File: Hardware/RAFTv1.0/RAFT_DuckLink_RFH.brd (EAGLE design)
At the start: 73.7 x 86.4 mm, 147 parts, among them J1 AMPHENOL_132134, J2 AMPHENOL_132134, J4 Micro-USB, J5 132134-15, J6 S2B-PH-K-S(LF)(SN), J8 POWER_JACK, Q1 SIA817EDJ, Q2 SI7288DP, Q4 SI7288DP, U1 SX1276, U10 PE4259, U2 MAX2771ETI+, U3 ESP32-D0WD, U4 W25Q16BVSSIG, U5 INTERFACE-CP2102-GMR(QFN28), U6 PE4259, U7 SP0503BAHT, U8 BQ24650RVAR, U9 TPS63070RNMT, Y1 32.768kHz

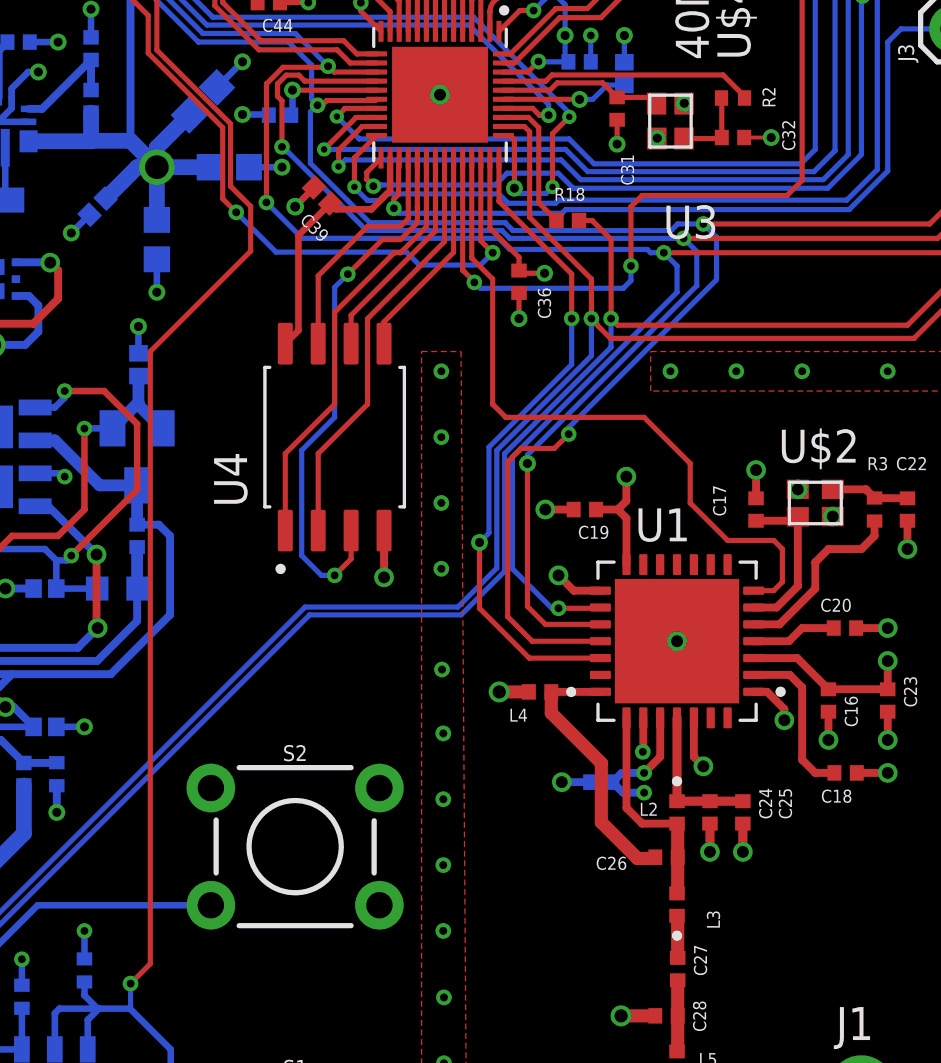
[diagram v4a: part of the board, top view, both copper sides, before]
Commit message: added connection SX1276 interrupt (remapped SX_RST to button)
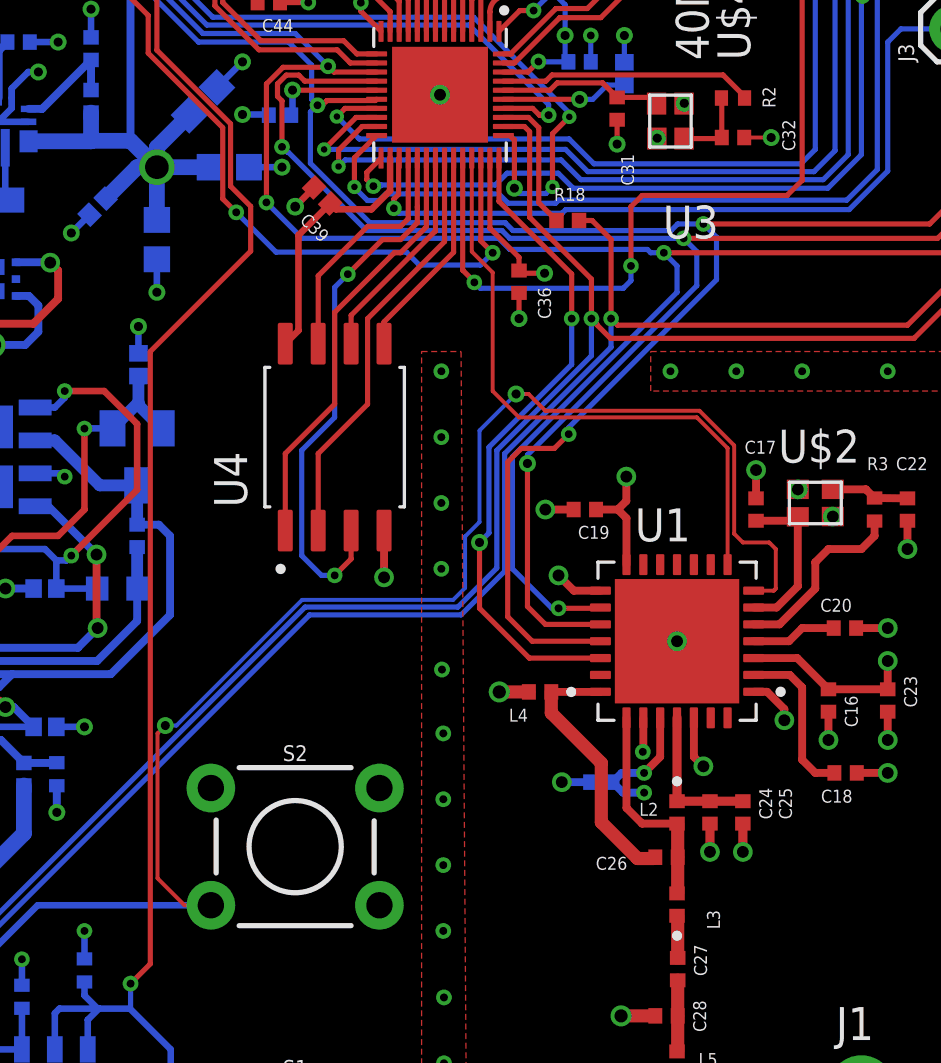
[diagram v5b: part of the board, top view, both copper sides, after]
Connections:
- removed net N$44: Q4.5, Q4.6, R24.1, S2.3
- new net SX_INT: U1.8, U3.35
- net SX_RST: now also Q4.5, Q4.6, R24.1, S2.3; no longer U3.35
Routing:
- net SX_RST: track 26.7 -> 63.3 mm, vias 0 -> 2
- net SX_INT: track 0.00 -> 23.8 mm
- net N$44: track 15.9 -> 0.00 mm
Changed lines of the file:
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@@
 <attribute name="MF" value="Murata" x="-16.51" y="-22.606" size="1.778" layer="27" rot="R270" display="off"/>
 <attribute name="MP" value="GCM1555C1H150JA16D" x="-16.51" y="-22.606" size="1.778" layer="27" rot="R270" display="off"/>
-<attribute name="NAME" x="56.764" y="35.494" size="0.5" layer="25" rot="R270"/>
+<attribute name="NAME" x="57.978" y="36.698" size="0.5" layer="25"/>
 <attribute name="PACKAGE" value="1005 Taiyo Yuden" x="-16.51" y="-22.606" size="1.778" layer="27" rot="R270" display="off"/>
 <attribute name="VALUE" x="57.79" y="35.494" size="0.5" layer="27" rot="R270" align="top-left"/>
@@
 <vertex x="47.0408" y="40.64"/>
 <vertex x="47.29330625" y="4.52269375"/>
-<vertex x="47.29330625" y="4.52269375"/>
 <vertex x="47.29330625" y="4.064"/>
 <vertex x="70.612" y="4.064"/>
@@
 <signal name="SX_RST">
 <contactref element="U1" pad="7"/>
-<contactref element="U3" pad="35"/>
-<wire x1="57.3278" y1="33.3502" x2="59.1058" y2="33.3502" width="0.2" layer="1"/>
-<wire x1="59.1058" y1="33.3502" x2="59.436" y2="33.02" width="0.2" layer="1"/>
-<wire x1="59.436" y1="33.02" x2="59.436" y2="31.75" width="0.2" layer="1"/>
-<wire x1="59.436" y1="31.75" x2="59.1" y2="31.414" width="0.2" layer="1"/>
-<wire x1="59.1" y1="31.414" x2="58.327" y2="31.414" width="0.2" layer="1"/>
-<wire x1="55.88" y1="34.798" x2="55.88" y2="36.322" width="0.2" layer="1"/>
-<wire x1="55.88" y1="36.322" x2="54.102" y2="38.1" width="0.2" layer="1"/>
-<wire x1="57.3278" y1="33.3502" x2="55.88" y2="34.798" width="0.2" layer="1"/>
-<wire x1="48.26" y1="43.434" x2="47.453" y2="44.241" width="0.2" layer="1"/>
-<wire x1="47.453" y1="48.101" x2="47.453" y2="44.241" width="0.2" layer="1"/>
-<wire x1="54.102" y1="38.1" x2="48.768" y2="38.1" width="0.2" layer="1"/>
-<wire x1="48.26" y1="38.608" x2="48.768" y2="38.1" width="0.2" layer="1"/>
-<wire x1="48.26" y1="38.608" x2="48.26" y2="43.434" width="0.2" layer="1"/>
+<contactref element="Q4" pad="5"/>
+<contactref element="Q4" pad="6"/>
+<contactref element="S2" pad="3"/>
+<contactref element="R24" pad="1"/>
+<wire x1="28.829" y1="13.717" x2="28.829" y2="17.399" width="0.254" layer="16" grouprefs="POWER"/>
+<wire x1="28.829" y1="17.399" x2="30.7086" y2="19.2786" width="0.254" layer="16" grouprefs="POWER"/>
+<wire x1="30.099" y1="13.717" x2="30.099" y2="15.303" width="0.254" layer="16" grouprefs="POWER"/>
+<wire x1="30.7086" y1="19.2786" x2="37.3888" y2="19.2786" width="0.254" layer="16"/>
+<wire x1="28.829" y1="13.717" x2="30.099" y2="13.717" width="0.254" layer="16"/>
+<wire x1="58.327" y1="31.414" x2="59.1" y2="31.414" width="0.1524" layer="1"/>
+<wire x1="59.1" y1="31.414" x2="59.182" y2="31.496" width="0.1524" layer="1"/>
+<wire x1="59.182" y1="31.496" x2="59.182" y2="33.02" width="0.1524" layer="1"/>
+<wire x1="59.182" y1="33.02" x2="58.928" y2="33.274" width="0.1524" layer="1"/>
+<wire x1="58.928" y1="33.274" x2="57.912" y2="33.274" width="0.1524" layer="1"/>
+<wire x1="49.161153125" y1="39.001153125" x2="49.644846875" y2="39.001153125" width="0.1524" layer="1"/>
+<wire x1="50.292" y1="38.354" x2="49.644846875" y2="39.001153125" width="0.1524" layer="1"/>
+<wire x1="57.576" y1="37.0172125" x2="56.2392125" y2="38.354" width="0.1524" layer="1"/>
+<wire x1="56.2392125" y1="38.354" x2="50.292" y2="38.354" width="0.1524" layer="1"/>
+<wire x1="57.912" y1="33.274" x2="57.576" y2="33.61" width="0.1524" layer="1"/>
+<wire x1="57.576" y1="33.61" x2="57.576" y2="37.0172125" width="0.1524" layer="1"/>
+<via x="49.161153125" y="39.001153125" extent="1-16" drill="0.35"/>
+<wire x1="49.161153125" y1="39.001153125" x2="47.752" y2="37.592" width="0.1524" layer="16"/>
+<wire x1="47.752" y1="34.06030625" x2="47.196" y2="33.50430625" width="0.1524" layer="16"/>
+<wire x1="47.196" y1="31.5194" x2="46.736" y2="31.0594" width="0.1524" layer="16"/>
+<wire x1="47.196" y1="33.50430625" x2="47.196" y2="31.5194" width="0.1524" layer="16"/>
+<via x="35.6318" y="26.21029375" extent="1-16" drill="0.35"/>
+<wire x1="46.736" y1="31.0594" x2="40.908" y2="31.0594" width="0.1524" layer="16"/>
+<wire x1="36.05889375" y1="26.21029375" x2="35.6318" y2="26.21029375" width="0.1524" layer="16"/>
+<wire x1="40.908" y1="31.0594" x2="36.05889375" y2="26.21029375" width="0.1524" layer="16"/>
+<wire x1="35.6318" y1="26.21029375" x2="35.3298" y2="25.90829375" width="0.1524" layer="1"/>
+<wire x1="35.3298" y1="25.90829375" x2="35.3298" y2="20.32" width="0.1524" layer="1"/>
+<wire x1="35.3298" y1="20.32" x2="36.3712" y2="19.2786" width="0.1524" layer="1"/>
+<wire x1="36.3712" y1="19.2786" x2="37.3888" y2="19.2786" width="0.1524" layer="1"/>
+<wire x1="47.752" y1="37.592" x2="47.752" y2="34.06030625" width="0.1524" layer="16"/>
 </signal>
 <signal name="N$10">
@@
 <wire x1="22.5552" y1="22.9108" x2="23.876" y2="21.59" width="0.3048" layer="16"/>
 </signal>
-<signal name="N$44">
-<contactref element="Q4" pad="5"/>
-<contactref element="Q4" pad="6"/>
-<contactref element="S2" pad="3"/>
-<contactref element="R24" pad="1"/>
-<wire x1="28.829" y1="13.717" x2="28.829" y2="17.399" width="0.254" layer="16" grouprefs="POWER"/>
-<wire x1="28.829" y1="17.399" x2="30.7086" y2="19.2786" width="0.254" layer="16" grouprefs="POWER"/>
-<wire x1="30.099" y1="13.717" x2="30.099" y2="15.303" width="0.254" layer="16" grouprefs="POWER"/>
-<wire x1="30.7086" y1="19.2786" x2="37.3888" y2="19.2786" width="0.254" layer="16"/>
-<wire x1="28.829" y1="13.717" x2="30.099" y2="13.717" width="0.254" layer="16"/>
-</signal>
 <signal name="V_BAT">
 <contactref element="C67" pad="2"/>
@@
 <wire x1="9.398" y1="28.448" x2="7.62" y2="30.226" width="0.8128" layer="1"/>
 </signal>
+<signal name="SX_INT">
+<contactref element="U1" pad="8"/>
+<contactref element="U3" pad="35"/>
+<wire x1="47.453" y1="48.101" x2="47.453" y2="44.495" width="0.1524" layer="1"/>
+<wire x1="48.26" y1="43.688" x2="48.26" y2="39.116" width="0.1524" layer="1"/>
+<wire x1="47.453" y1="44.495" x2="48.26" y2="43.688" width="0.1524" layer="1"/>
+<wire x1="48.26" y1="39.116" x2="49.276" y2="38.1" width="0.1524" layer="1"/>
+<wire x1="49.276" y1="38.1" x2="56.134" y2="38.1" width="0.1524" layer="1"/>
+<wire x1="56.134" y1="38.1" x2="57.322" y2="36.912" width="0.1524" layer="1"/>
+<wire x1="57.322" y1="36.912" x2="57.322" y2="32.419" width="0.1524" layer="1"/>
+</signal>
 </signals>
